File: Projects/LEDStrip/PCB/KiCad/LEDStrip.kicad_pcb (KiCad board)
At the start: 2 copper layers, 49 parts, among them J1 USB_C_Receptacle_USB2.0_16P, J2 Conn_01x04, Q1 IRFML8244, Q2 IRFML8244, Q3 IRFML8244, SW1 SW_DIP_x01, SW2 SW_DIP_x01, U1 MSGEQ7, U2 ESP32-S3-WROOM-1, U3 LM2596S-5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

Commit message: pcb changes
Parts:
- added C15: 22nF - 1uF, Capacitor_Tantalum_SMD:CP_EIA-3216-18_Kemet-A, F.Cu at (110.2, 91.4)
- added C16: 2.2uF, Capacitor_Tantalum_SMD:CP_EIA-3216-18_Kemet-A, F.Cu at (115.7, 87.9)
- added C17: 0.47uF, Capacitor_Tantalum_SMD:CP_EIA-3216-18_Kemet-A, F.Cu at (119.2, 89.0)
- added C18: 0.1uF, Capacitor_Tantalum_SMD:CP_EIA-3216-18_Kemet-A, F.Cu at (115.7, 94.9)
- added C19: 1uF, Capacitor_Tantalum_SMD:CP_EIA-3216-18_Kemet-A, F.Cu at (110.2, 93.9)
- added H1: Hole_Pad, MountingHole:MountingHole_3.2mm_M3_ISO7380_Pad, F.Cu at (106.4, 44.5)
- added H2: Hole_Pad, MountingHole:MountingHole_3.2mm_M3_ISO7380_Pad, F.Cu at (203.0, 50.6)
- added H3: Hole_Pad, MountingHole:MountingHole_3.2mm_M3_ISO7380_Pad, F.Cu at (106.0, 136.4)
- added H4: Hole_Pad, MountingHole:MountingHole_3.2mm_M3_ISO7380_Pad, F.Cu at (200.2, 136.0)
- added J3: LED ADDR, Connector_JST:JST_SH_SM03B-SRSS-TB_1x03-1MP_P1.00mm_Horizontal, F.Cu at (157.0, 42.9)
- added J4: LED MATRIX, Connector_JST:JST_SH_SM05B-SRSS-TB_1x05-1MP_P1.00mm_Horizontal, F.Cu at (148.7, 42.9)
- added J5: Barrel Jack, Connector_BarrelJack:BarrelJack_Kycon_KLDX-0202-xC_Horizontal, F.Cu at (151.1, 126.0)
- added J6: SSD1306, Connector_PinHeader_2.54mm:PinHeader_1x04_P2.54mm_Vertical, F.Cu at (198.3, 121.0)
- added J7: TFT, Connector_PinHeader_2.54mm:PinHeader_1x08_P2.54mm_Vertical, F.Cu at (202.7, 110.8)
- added JP1: TFT BKL, Jumper:SolderJumper-3_P1.3mm_Open_RoundedPad1.0x1.5mm_NumberLabels, F.Cu at (198.8, 113.7)
- added JP2: MIC GAIN, Jumper:SolderJumper-3_P1.3mm_Open_RoundedPad1.0x1.5mm_NumberLabels, F.Cu at (125.7, 88.4)
- added JP3: ATT : REL, Jumper:SolderJumper-3_P1.3mm_Open_RoundedPad1.0x1.5mm_NumberLabels, F.Cu at (125.4, 93.5)
- added MK1: CMA-4544PF-W, CMA-4544PF-W:MIC_CMA-4544PF-W, F.Cu at (133.7, 90.9)
- added R10: 330, Resistor_SMD:R_0603_1608Metric, F.Cu at (128.3, 63.1)
- added R11: 1k, Resistor_SMD:R_0603_1608Metric, F.Cu at (127.6, 69.2)
- added R12: 100k, Resistor_SMD:R_0603_1608Metric, F.Cu at (121.2, 89.9)
- added R13: 150k, Resistor_SMD:R_0603_1608Metric, F.Cu at (119.7, 94.9)
- added R14: 2.2k, Resistor_SMD:R_0603_1608Metric, F.Cu at (119.7, 93.4)
- added R9: 330, Resistor_SMD:R_0603_1608Metric, F.Cu at (157.8, 48.3)
- added SW3: CMD BTN, Connector_Hirose:Hirose_DF13-04P-1.25DSA_1x04_P1.25mm_Vertical, F.Cu at (137.2, 74.8)
- added U6: MAX9814, Package_DFN_QFN:DFN-14-1EP_3x3mm_P0.4mm_EP1.78x2.35mm, F.Cu at (115.7, 91.4)
- J1: value USB_C_Receptacle_USB2.0_16P -> USB_C
- J2: value Conn_01x04 -> RGB LED; footprint Connector_Molex:Molex_KK-254_AE-6410-04A_1x04_P2.54mm_Vertical -> Connector_JST:JST_SH_SM04B-SRSS-TB_1x04-1MP_P1.00mm_Horizontal
- Q1, Q2, Q3: footprint Package_DirectFET:DirectFET_SB -> Package_TO_SOT_SMD:SOT-23
- moved Q3 173.5 mm to (192.9, 132.1)
- moved Q1 171.9 mm to (189.0, 127.1)
- moved Q2 171.5 mm to (188.8, 132.0)
- moved J2 171.5 mm to (190.6, 137.2)
- moved C6 158.2 mm to (172.8, 50.1)
- moved C7 158.1 mm to (172.7, 53.0)
- moved C8 153.0 mm to (172.6, 47.2)
- moved R8 152.3 mm to (194.8, 117.1), turned to 90 degrees
- moved SW2 152.2 mm to (191.2, 116.9)
- moved C14 148.0 mm to (187.5, 116.8), turned to 90 degrees
- moved CIN1 147.0 mm to (163.2, 112.0)
- moved CIN2 147.0 mm to (163.2, 119.5)
- moved C5 146.9 mm to (156.4, 114.4)
- moved U2 145.9 mm to (184.4, 52.6)
- moved R4 145.9 mm to (169.6, 50.1)
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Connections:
- R6 pad 2: AUDIO_IN -> AUDIO
- U2 pad 11: unconnected-(U2-IO18-Pad11) -> DISP_SDA
- U2 pad 17: unconnected-(U2-IO9-Pad17) -> DISP_SCL
- U2 pad 18: unconnected-(U2-IO10-Pad18) -> TFT_MOSI
- U2 pad 19: unconnected-(U2-IO11-Pad19) -> TFT_SCLK
- U2 pad 20: unconnected-(U2-IO12-Pad20) -> TFT_RST
- U2 pad 21: unconnected-(U2-IO13-Pad21) -> TFT_DC
- U2 pad 22: unconnected-(U2-IO14-Pad22) -> TFT_CS
- U2 pad 24: unconnected-(U2-IO47-Pad24) -> MAT_CS
- U2 pad 25: unconnected-(U2-IO48-Pad25) -> MAT_CLK
- U2 pad 26: unconnected-(U2-IO45-Pad26) -> MAT_DIN
- U2 pad 30: RGB_G -> unconnected-(U2-IO37-Pad30)
- U2 pad 31: RGB_R -> unconnected-(U2-IO38-Pad31)
- U2 pad 33: unconnected-(U2-IO40-Pad33) -> RGB_R
- U2 pad 34: unconnected-(U2-IO41-Pad34) -> RGB_G
- U2 pad 35: unconnected-(U2-IO42-Pad35) -> LED_ADDR
- U2 pad 38: unconnected-(U2-IO2-Pad38) -> EQ_STROBE
- U2 pad 39: unconnected-(U2-IO1-Pad39) -> EQ_DATA
- U2 pad 4: unconnected-(U2-IO4-Pad4) -> CMD_BTN
- U2 pad 5: unconnected-(U2-IO5-Pad5) -> EQ_RESET
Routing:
- net <NO NET>: track 0.00 -> 263.6 mm
- net VCC_5V: track 0.00 -> 61.7 mm
- net VCC_12V: track 0.00 -> 60.3 mm
- net ESP_3V3: track 0.00 -> 40.6 mm
- net PER_5V: track 0.00 -> 33.0 mm, vias 0 -> 2
- net Net-(D7-K): track 0.00 -> 23.1 mm
- net Net-(D1-A): track 0.00 -> 16.6 mm
- net Net-(D3-K): track 0.00 -> 15.8 mm
- net LED_R: track 0.00 -> 14.6 mm, vias 0 -> 2
- net CHIP_PU: track 0.00 -> 11.9 mm
- net D+: track 0.00 -> 9.07 mm
- net GPIO0: track 0.00 -> 7.44 mm
- net LED_G: track 0.00 -> 6.97 mm
- net VDD_EQ: track 0.00 -> 6.73 mm
- net D-: track 0.00 -> 6.56 mm
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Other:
- board outline added: 104.2 x 101.4 mm
- board text added: "LED Strip"
- board text added: "Power"

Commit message: pcb changes
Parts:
- removed CIN2: 330uF, Capacitor_Tantalum_SMD:CP_EIA-7360-38_Kemet-E
- added G***: LOGO, LOGO, F.Cu at (129.9, 69.7)
- added R15: 330, Resistor_SMD:R_0603_1608Metric, F.Cu at (165.9, 77.8)
- added R16: 1k, Resistor_SMD:R_0603_1608Metric, F.Cu at (172.9, 70.3)
- R11: value 1k -> 330
- SW3: footprint Connector_Hirose:Hirose_DF13-04P-1.25DSA_1x04_P1.25mm_Vertical -> IguanaLibrary:SW_RGB_JST_SH
- moved J6 106.0 mm to (111.0, 60.9)
- moved J7 94.3 mm to (111.0, 88.8)
- moved JP1 86.6 mm to (115.7, 89.3)
- moved R8 69.0 mm to (142.4, 72.2)
- moved C13 69.0 mm to (135.2, 65.9)
- moved SW1 69.0 mm to (139.0, 65.9)
- moved SW2 69.0 mm to (138.9, 72.0)
- moved C14 69.0 mm to (135.1, 71.9)
- moved R7 69.0 mm to (142.7, 65.9)
- moved J1 61.2 mm to (112.8, 80.3), turned to -90 degrees
- moved D1 56.4 mm to (118.4, 75.7), turned to -90 degrees
- moved R1 54.1 mm to (118.3, 79.7), turned to -90 degrees
- moved C1 53.3 mm to (121.2, 75.3), turned to -90 degrees
- moved R2 52.1 mm to (118.3, 84.0), turned to -90 degrees
- moved D5 51.2 mm to (121.2, 78.3), turned to -90 degrees
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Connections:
- R10 pad 1: <NO NET> -> Net-(R10-Pad1)
- R10 pad 2: Net-(SW3-K) -> RGB_R
- R11 pad 1: <NO NET> -> Net-(R11-Pad1)
- R11 pad 2: CMD_BTN -> RGB_G
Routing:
- net <NO NET>: track 263.6 -> 608.0 mm, vias 0 -> 6
- net ESP_3V3: track 40.6 -> 233.5 mm, vias 0 -> 11
- net PER_5V: track 33.0 -> 127.0 mm, vias 2 -> 3
- net VCC_12V: track 60.3 -> 147.9 mm, vias 0 -> 2
- net RGB_R: track 0.00 -> 78.2 mm
- net RGB_G: track 0.00 -> 66.5 mm, vias 0 -> 2
- net TFT_DC: track 0.00 -> 65.6 mm, vias 0 -> 1
- net RGB_B: track 0.00 -> 62.4 mm, vias 0 -> 4
- net TFT_CS: track 0.00 -> 58.9 mm, vias 0 -> 1
- net EQ_RESET: track 0.00 -> 57.7 mm, vias 0 -> 1
- net TFT_SCLK: track 0.00 -> 55.4 mm, vias 0 -> 1
- net DISP_SCL: track 0.00 -> 53.8 mm, vias 0 -> 2
- net MAT_DIN: track 0.00 -> 53.1 mm, vias 0 -> 2
- net TFT_MOSI: track 0.00 -> 53.0 mm, vias 0 -> 1
- net TFT_RST: track 0.00 -> 52.3 mm, vias 0 -> 1
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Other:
- board size 104.2 x 101.4 mm -> 67 x 80.9 mm

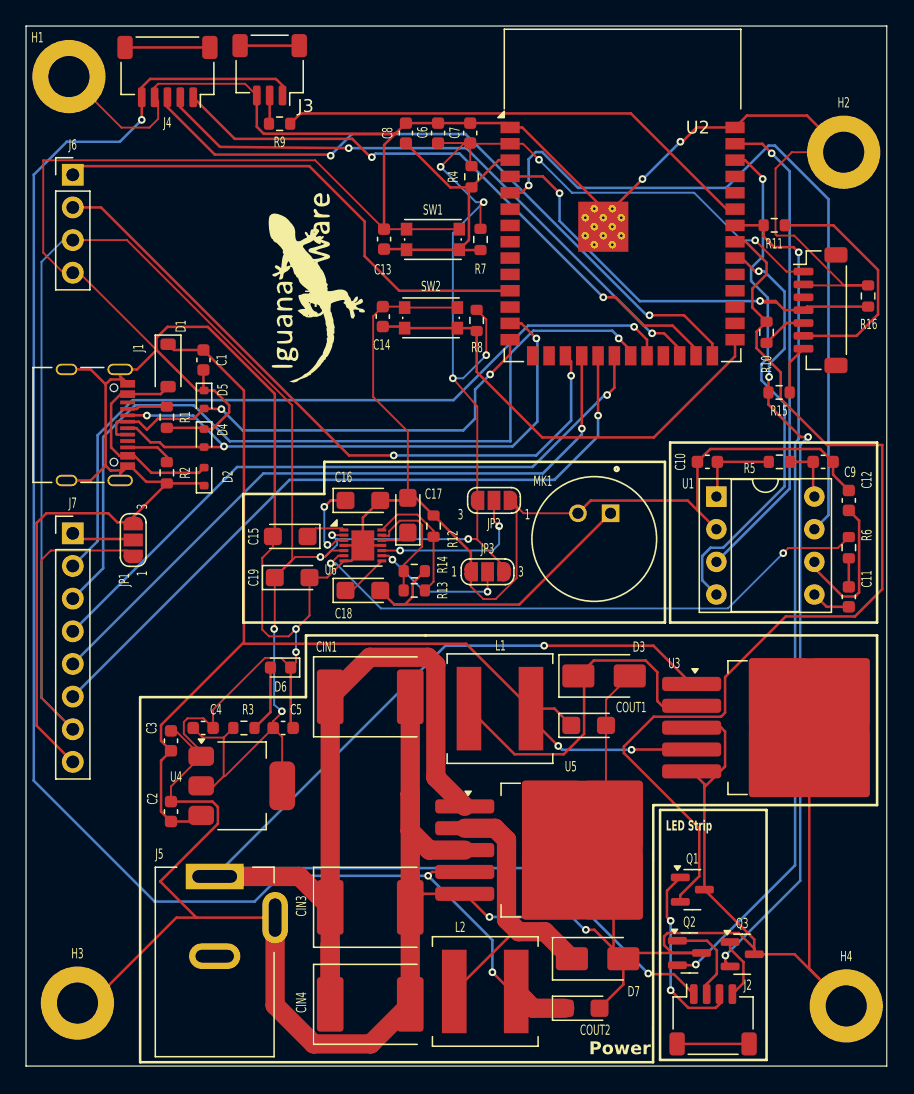
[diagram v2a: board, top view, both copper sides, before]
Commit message: PCB changes - almost complete, still needs copper fill
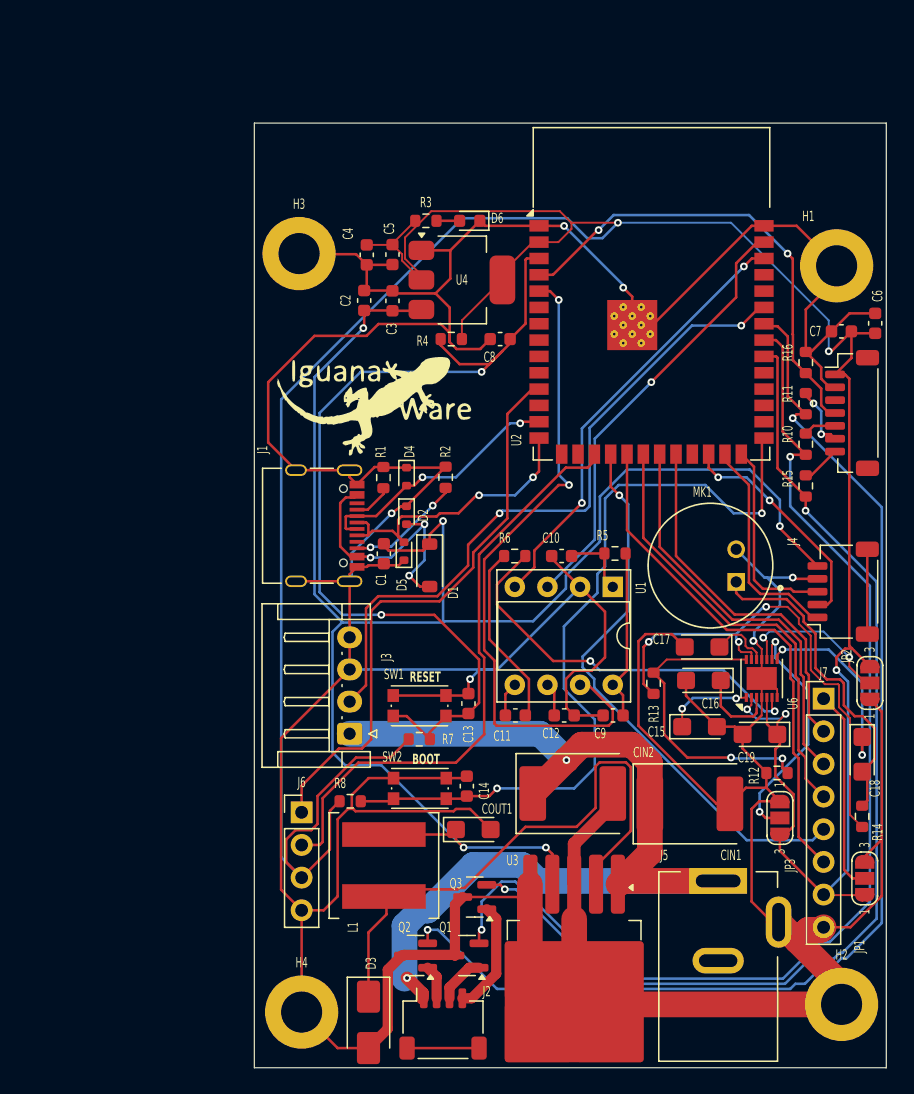
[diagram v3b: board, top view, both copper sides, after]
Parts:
- removed CIN3, CIN4: 330uF, Capacitor_Tantalum_SMD:CP_EIA-7360-38_Kemet-E
- removed COUT2: 220uF, Capacitor_Tantalum_SMD:CP_EIA-3216-18_Kemet-A
- removed D7: SK32, Diode_SMD:D_SMA
- removed G***: LOGO, LOGO
- removed L2: 3uH, Inductor_SMD:L_Coilcraft_XAL7070-XXX
- removed R9: 330, Resistor_SMD:R_0603_1608Metric
- removed U5: LM2596S-5, Package_TO_SOT_SMD:TO-263-5_TabPin3
- added ?: LOGO, IguanaWare:IguanaWare, F.Cu at (134.4, 78.8)
- added CIN2: 330uF, Capacitor_Tantalum_SMD:CP_EIA-7360-38_Kemet-E, F.Cu at (149.9, 109.0)
- J3: footprint Connector_JST:JST_SH_SM03B-SRSS-TB_1x03-1MP_P1.00mm_Horizontal -> Connector_JST:JST_EH_S4B-EH_1x04_P2.50mm_Horizontal
- moved J4 66.3 mm to (170.9, 93.3), turned to 90 degrees
- moved H2 66.3 mm to (170.8, 125.4)
- moved JP1 62.7 mm to (172.6, 115.6)
- moved H1 61.5 mm to (170.4, 68.0)
- moved H3 60.8 mm to (128.6, 67.0)
- moved J7 59.8 mm to (169.4, 101.6)
- moved J6 52.7 mm to (128.8, 110.5)
- moved J3 52.0 mm to (132.5, 104.3), turned to 90 degrees
- moved U4 42.9 mm to (141.3, 69.0)
- moved C2 42.5 mm to (133.7, 70.7)
- moved H4 42.4 mm to (128.8, 126.0)
- moved R3 41.9 mm to (138.5, 64.5)
- moved C18 40.9 mm to (172.4, 106.0), turned to -90 degrees
- moved R14 39.7 mm to (172.4, 110.8), turned to 90 degrees
- moved R7 39.2 mm to (137.9, 104.8), turned to 180 degrees
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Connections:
- J3 pad 1: PER_5V -> VCC_12V
- J3 pad 2: Net-(J3-Pin_2) -> LED_ADDR
- J4 pad 5: PER_5V -> VCC_5V
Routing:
- net <NO NET>: track 608.0 -> 450.5 mm
- net PER_5V: track 127.0 -> 0.00 mm, vias 3 -> 0
- net VCC_12V: track 147.9 -> 80.3 mm
- net CHIP_PU: track 23.2 -> 72.2 mm, vias 0 -> 2
- net VCC_5V: track 89.6 -> 134.7 mm, vias 2 -> 5
- net MAT_DIN: track 53.1 -> 15.5 mm, vias 2 -> 0
- net TFT_DC: track 65.6 -> 31.5 mm, vias 1 -> 0
- net D-: track 51.5 -> 19.9 mm, vias 3 -> 2
- net MAT_CLK: track 48.0 -> 17.2 mm, vias 2 -> 0
- net TFT_CS: track 58.9 -> 28.4 mm, vias 1 -> 0
- net MAT_CS: track 48.0 -> 17.9 mm
- net Net-(U6-MICBIAS): track 9.66 -> 39.5 mm, vias 0 -> 3
- net RGB_G: track 66.5 -> 93.1 mm
- net GPIO0: track 36.7 -> 62.0 mm, vias 0 -> 2
- net Net-(D7-K): track 23.1 -> 0.00 mm
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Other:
- board size 67 x 80.9 mm -> 49.2 x 73.5 mm
- board text added: "BOOT"
- board text added: "RESET"
- board text removed: "LED Strip"
- board text removed: "Power"

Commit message: pcb final
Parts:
- moved H3 0.95 mm to (128.6, 68.0)
- moved H2 0.63 mm to (170.6, 126.0)
- moved H1 0.46 mm to (170.9, 68.0)
- moved H4 0.07 mm to (128.9, 126.0)
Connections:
- C1 pad 2: <NO NET> -> GND
- C10 pad 2: <NO NET> -> GND
- C12 pad 2: <NO NET> -> GND
- C2 pad 2: <NO NET> -> GND
- C3 pad 2: <NO NET> -> GND
- C4 pad 2: <NO NET> -> GND
- C5 pad 2: <NO NET> -> GND
- C6 pad 2: <NO NET> -> GND
- C7 pad 2: <NO NET> -> GND
- C8 pad 2: <NO NET> -> GND
- C9 pad 1: <NO NET> -> GND
- D2 pad 1: <NO NET> -> GND
- D4 pad 1: <NO NET> -> GND
- D5 pad 1: <NO NET> -> GND
- D6 pad 1: <NO NET> -> GND
- H1 pad 1: <NO NET> -> GND
- H2 pad 1: <NO NET> -> GND
- H3 pad 1: <NO NET> -> GND
- H4 pad 1: <NO NET> -> GND
- J1 pad A1: <NO NET> -> GND
- J1 pad A12: <NO NET> -> GND
- J1 pad B1: <NO NET> -> GND
- J1 pad B12: <NO NET> -> GND
- J1 pad S1: <NO NET> -> GND
- J3 pad 3: <NO NET> -> GND
- J3 pad 4: <NO NET> -> GND
- J4 pad 4: <NO NET> -> GND
- J5 pad 3: <NO NET> -> GND
- J6 pad 4: <NO NET> -> GND
- J7 pad 8: <NO NET> -> GND
- JP1 pad 3: <NO NET> -> GND
- Q1 pad 3: <NO NET> -> GND
- Q2 pad 3: <NO NET> -> GND
- Q3 pad 3: <NO NET> -> GND
- R1 pad 2: <NO NET> -> GND
- R16 pad 1: <NO NET> -> GND
- R2 pad 2: <NO NET> -> GND
- SW3 pad C2: <NO NET> -> GND
- U1 pad 2: <NO NET> -> GND
- U2 pad 1: <NO NET> -> GND
- U2 pad 40: <NO NET> -> GND
- U2 pad 41: <NO NET> -> GND
- U4 pad 1: <NO NET> -> GND
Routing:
- net GND: track 0.00 -> 325.0 mm, vias 0 -> 3
- net <NO NET>: track 450.5 -> 213.1 mm
- net CHIP_PU: track 72.2 -> 66.9 mm
- net EQ_RESET: track 52.3 -> 47.7 mm
- added copper zone on B.Cu, net GND
- added copper zone on F.Cu, net GND

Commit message: checks and finishing
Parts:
- added G***: LOGO, IguanaWare:Iguana, B.Cu at (135.2, 114.6)
- J1: value USB_C -> USB C
- JP2: value MIC GAIN -> GAIN
- SW1: value SW_DIP_x01 -> RESET
- moved J5 0.15 mm to (161.2, 116.0)
- moved J3 0.13 mm to (132.4, 104.3)
- moved J1 0.13 mm to (130.5, 88.2)
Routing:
- net VCC_5V: track 134.7 -> 136.3 mm
- net Net-(D1-A): track 21.3 -> 22.2 mm
- net ESP_3V3: track 243.4 -> 244.2 mm
- net D-: track 19.9 -> 20.4 mm
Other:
- board text added: "LED MATRIX"
- board text added: "MIC"
- board text removed: "RESET"
